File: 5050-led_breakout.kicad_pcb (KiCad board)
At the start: 2 copper layers, 3 parts, among them J1 1x3 Header, J2 1x3 Header

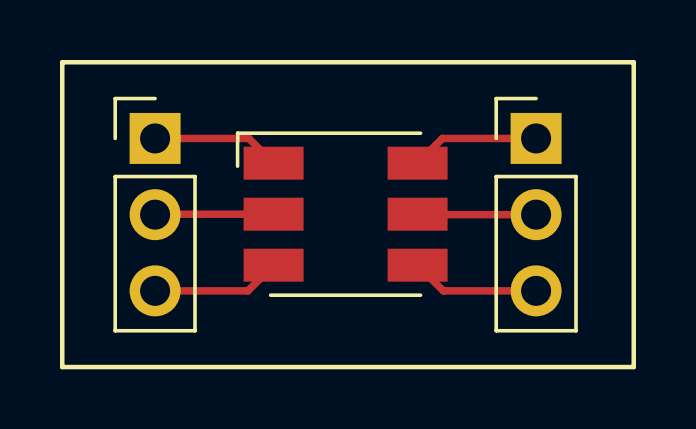
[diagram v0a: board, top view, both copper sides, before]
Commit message: Fixed edge layer type
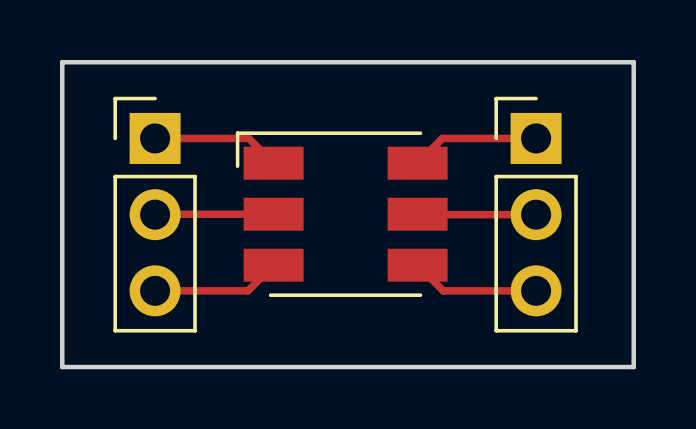
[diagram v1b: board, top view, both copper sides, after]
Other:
- board outline added: 19.1 x 10.2 mm
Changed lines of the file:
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@@
   )
   (gr_rect (start 130.81 96.52) (end 149.86 106.68)
-    (stroke (width 0.15) (type solid)) (fill none) (layer "F.SilkS"))
+    (stroke (width 0.15) (type solid)) (fill none) (layer "Edge.Cuts"))
   (segment (start 137.03 99.06) (end 137.855 99.885) (width 0.25) (layer "F.Cu") (net 1))
   (segment (start 133.905 99.06) (end 137.03 99.06) (width 0.25) (layer "F.Cu") (net 1))
